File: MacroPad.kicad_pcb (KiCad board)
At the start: 2 copper layers, 99.1 x 99.7 mm, 36 parts, among them J1 Conn_01x04_Socket, SW1 SW_Push_45deg, SW10 SW_Push_45deg, SW11 SW_Push_45deg, SW12 SW_Push_45deg, SW13 SW_Push_45deg, SW14 SW_Push_45deg, SW15 SW_Push_45deg, SW16 SW_Push_45deg, SW17 RotaryEncoder_Switch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

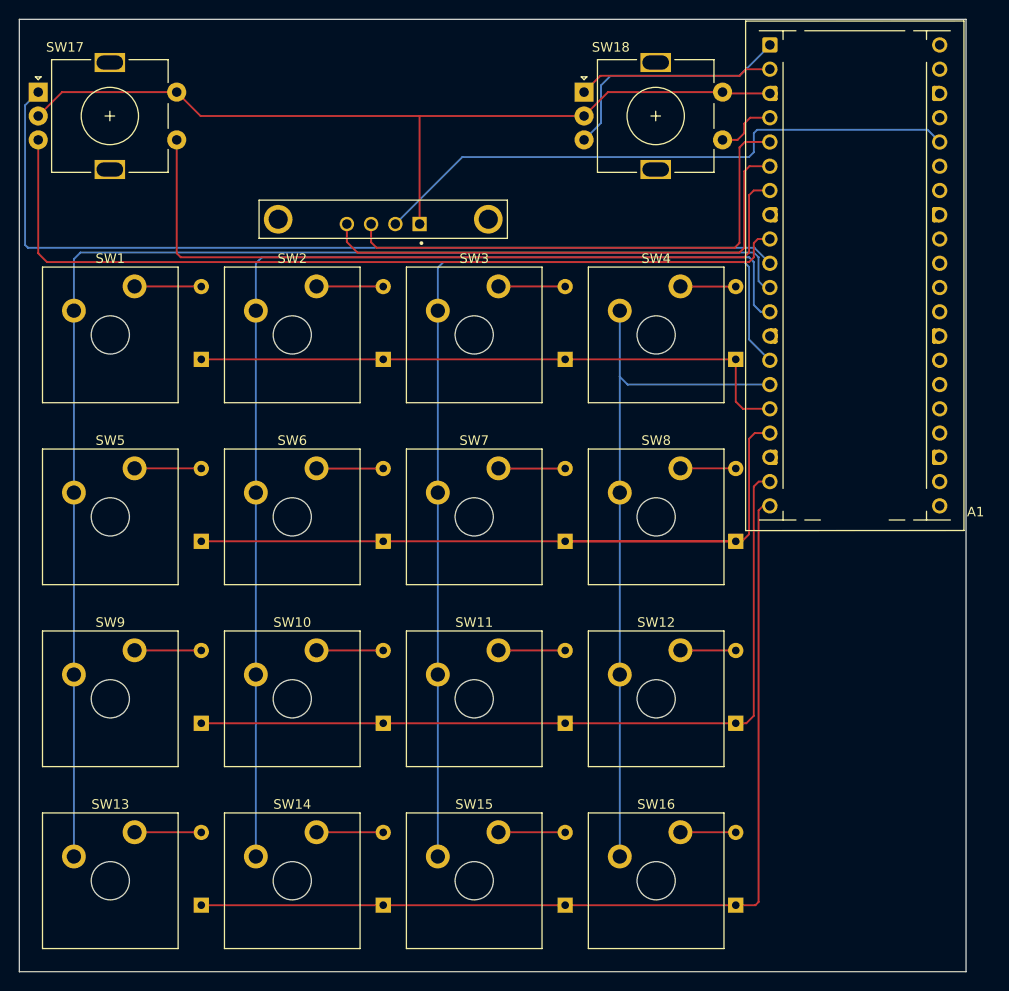
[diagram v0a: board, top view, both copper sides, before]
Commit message: Added QR code and name
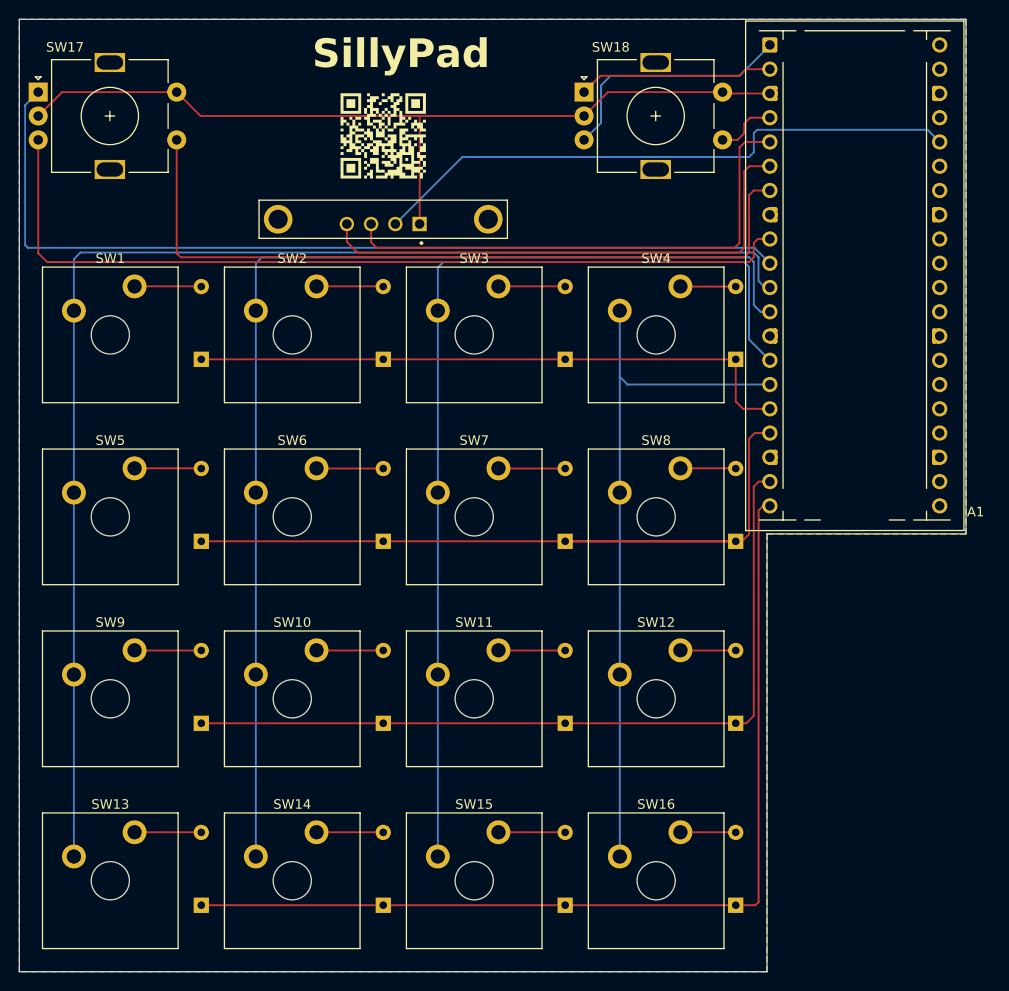
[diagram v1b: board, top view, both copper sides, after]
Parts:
- added G***: LOGO, SillyPad:QRCode, F.Cu at (76.2, 26.8)
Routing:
- added copper zone on B.Cu, net (none)
- added copper zone on F.Cu, net (none)
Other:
- outline, holes or cut-outs redrawn
- board text added: "SillyPad"

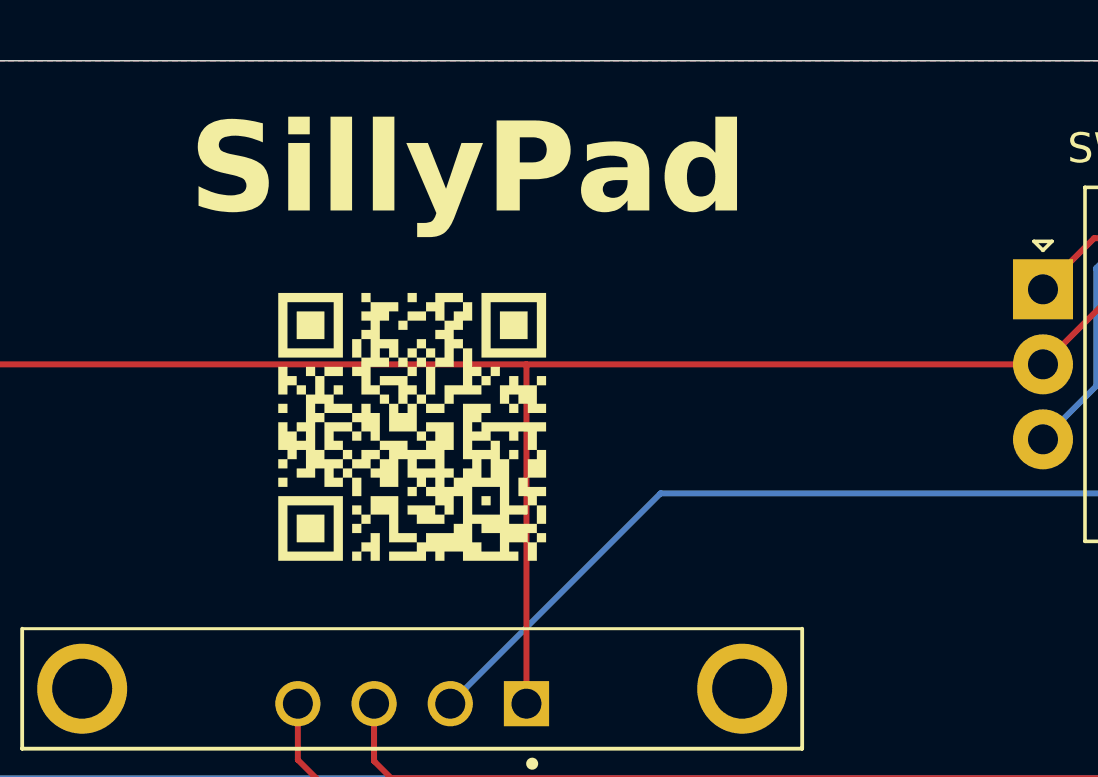
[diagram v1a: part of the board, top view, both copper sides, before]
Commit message: Added models & footprints to the repo
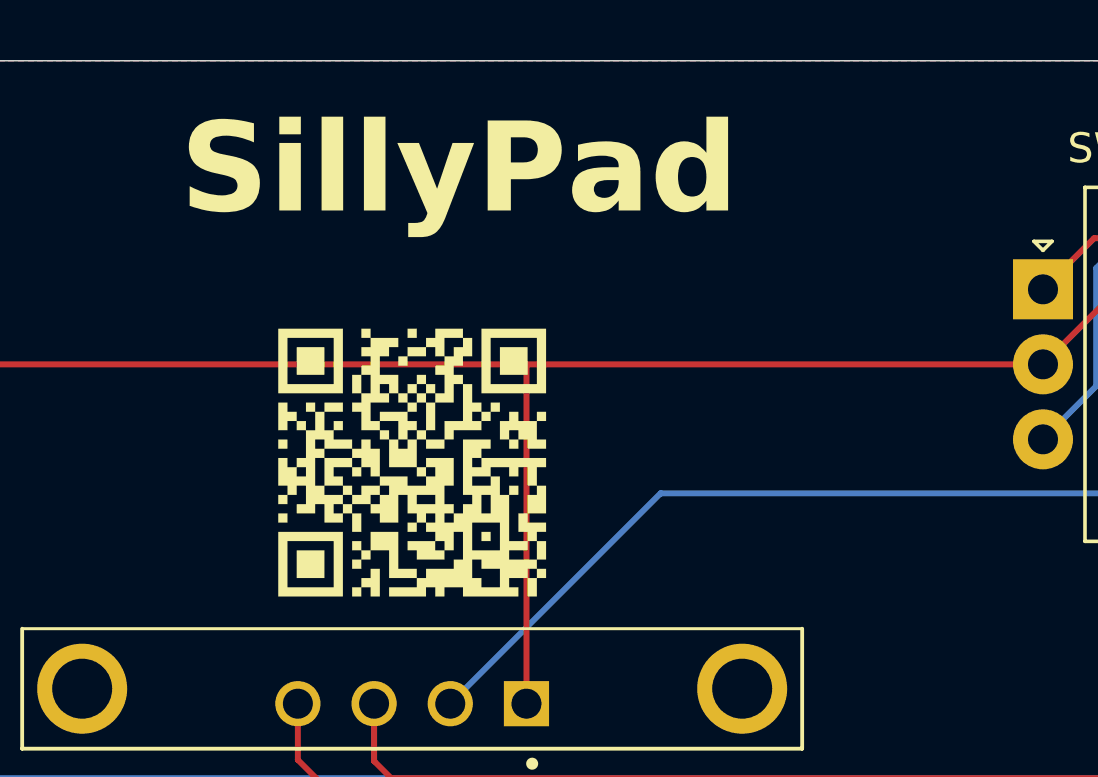
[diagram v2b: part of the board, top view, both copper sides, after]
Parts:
- A1: footprint Module:RaspberryPi_Pico_Common_THT -> SillyPad:RaspberryPi_Pico_Common_THT
- J1: footprint promicro:MODULE_DM-OLED096-636 -> SillyPad:MODULE_DM-OLED096-636
- SW1, SW10, SW11, SW12, SW13, SW14, SW15, SW16, SW2, SW3, SW4, SW5, SW6, SW7, SW8, SW9: footprint PCM_Switch_Keyboard_Cherry_MX:SW_Cherry_MX_Plate_1.00u -> SillyPad:SW_Cherry_MX_Plate_1.00u
- moved G*** 1.19 mm to (76.2, 28.0)
